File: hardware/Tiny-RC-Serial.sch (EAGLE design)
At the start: 16 parts, among them J1 ICSP, U1 ATTINY2313A, Y1 20Mhz

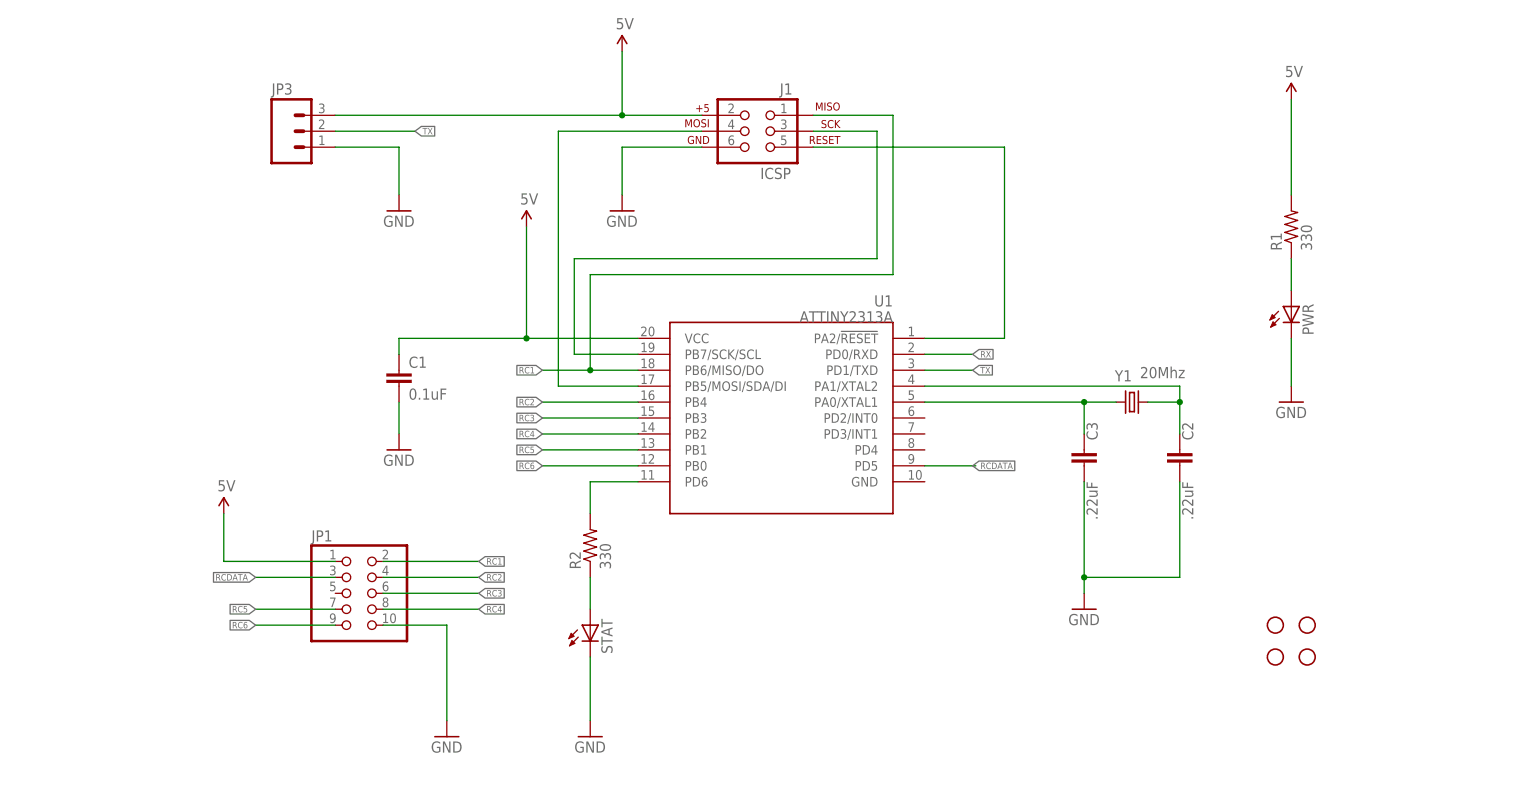
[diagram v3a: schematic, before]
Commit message: Update hardware to 3.1
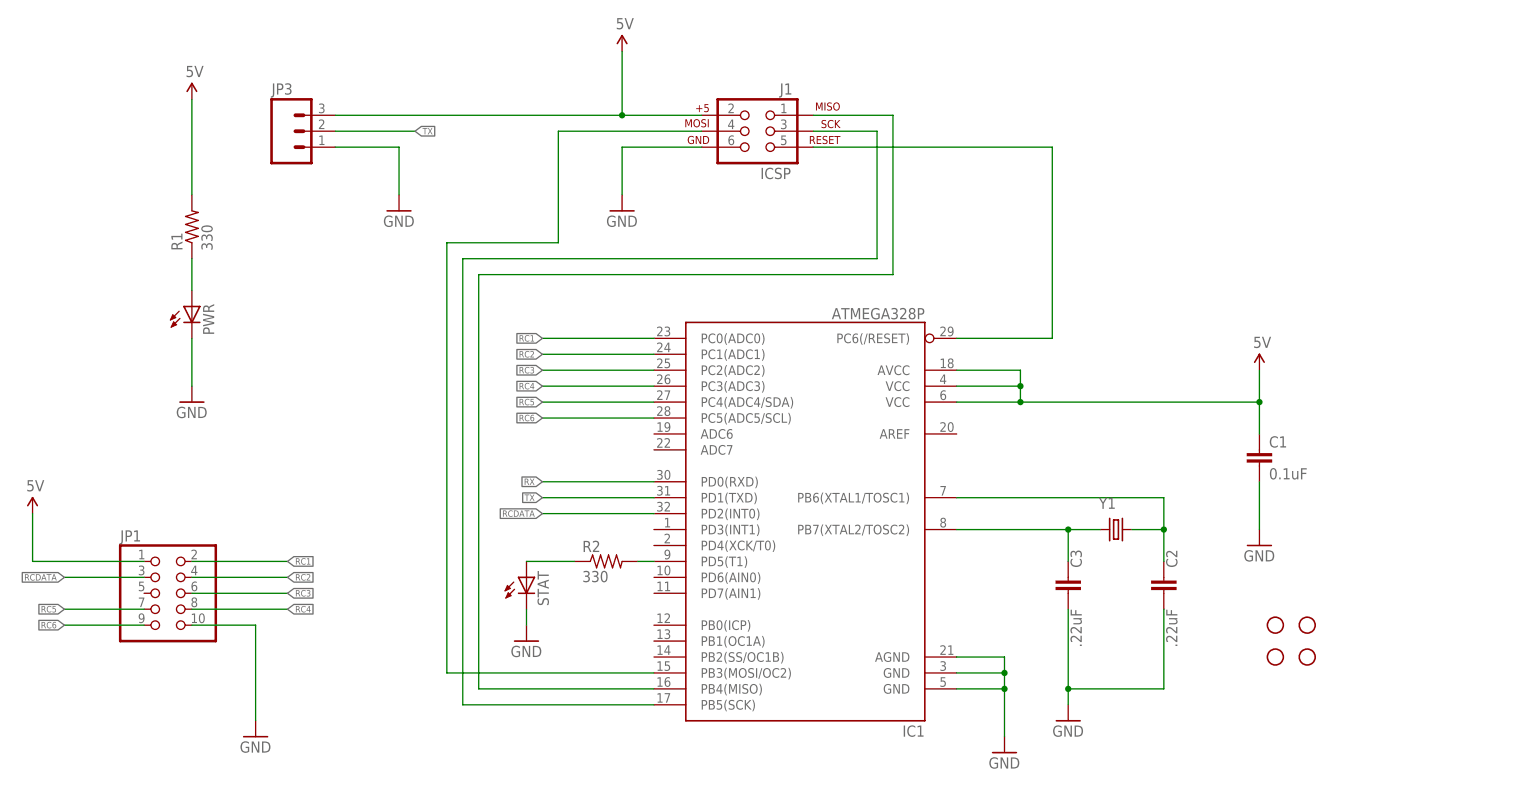
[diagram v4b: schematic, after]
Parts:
- removed U1: ATTINY2313A, SparkFun-DigitalIC:ATTINY2313A
- added IC1: ATMEGA328P, SparkFun-DigitalIC:ATMEGA328_SMT
- C1: device SparkFun:CAPPTH -> SparkFun-Capacitors:CAPKIT
- C2, C3: device SparkFun-Capacitors:CAP1206 -> SparkFun-Capacitors:CAPKIT
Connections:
- new net MISO: IC1.PB4(MISO), J1.1
- net 5V: now also IC1.AVCC, IC1.VCC@1, IC1.VCC@2; no longer U1.VCC
- net GND: now also IC1.AGND, IC1.GND@1, IC1.GND@2
- net MOSI: now also IC1.PB3(MOSI/OC2); no longer U1.PB5/MOSI/SDA/DI
- net N$1: now also IC1.PD5(T1); no longer U1.PD6
- net N$3: now also IC1.PB6(XTAL1/TOSC1); no longer U1.PA1/XTAL2
- net N$4: now also IC1.PB7(XTAL2/TOSC2); no longer U1.PA0/XTAL1
- net RC1: now also IC1.PC0(ADC0); no longer J1.1, U1.PB6/MISO/DO
- net RC2: now also IC1.PC1(ADC1); no longer U1.PB4
- net RC3: now also IC1.PC2(ADC2); no longer U1.PB3
- net RC4: now also IC1.PC3(ADC3); no longer U1.PB2
- net RC5: now also IC1.PC4(ADC4/SDA); no longer U1.PB1
- net RC6: now also IC1.PC5(ADC5/SCL); no longer U1.PB0
- net RCDATA: now also IC1.PD2(INT0); no longer U1.PD5
- net RESET: now also IC1.PC6(/RESET); no longer U1.PA2/!RESET
- net RX: now also IC1.PD0(RXD); no longer U1.PD0/RXD
- net SCK: now also IC1.PB5(SCK); no longer U1.PB7/SCK/SCL
- net TX: now also IC1.PD1(TXD); no longer U1.PD1/TXD
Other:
- moved on the sheet: C1, C2, C3, JP1, PWR, R1, R2, STAT, Y1
